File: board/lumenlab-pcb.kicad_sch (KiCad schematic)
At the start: 19 parts, among them J1 Barrel_Jack, SW1 SW_SPST, U1 MP2338

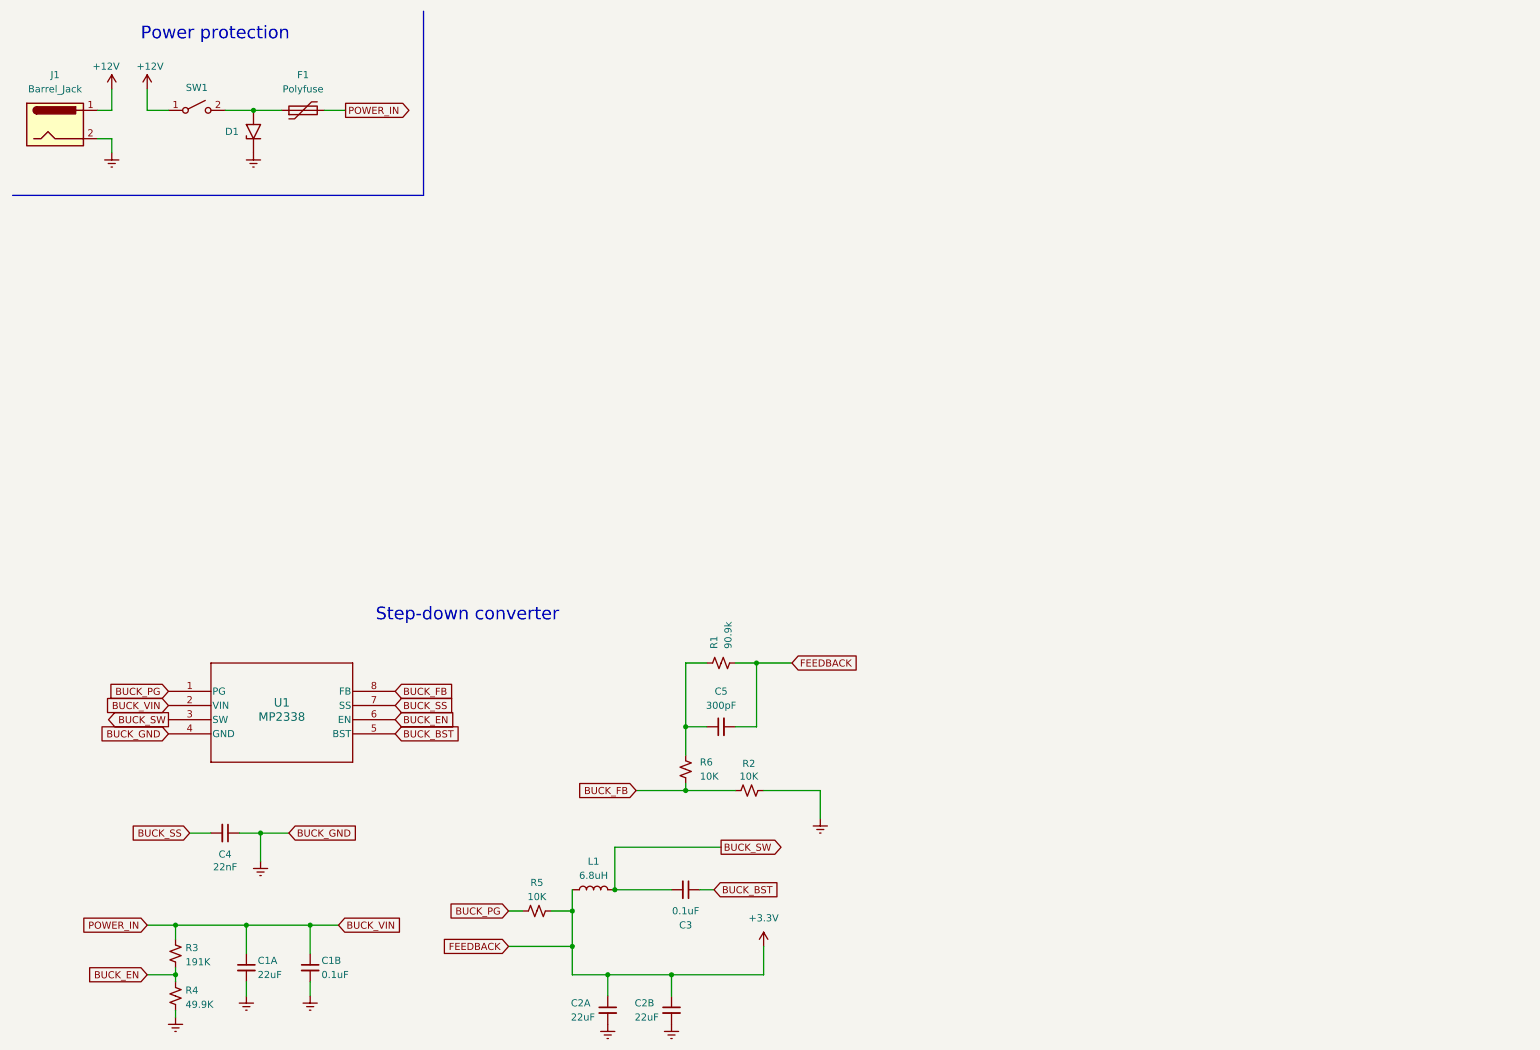
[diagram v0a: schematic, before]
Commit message: Move vendor lib
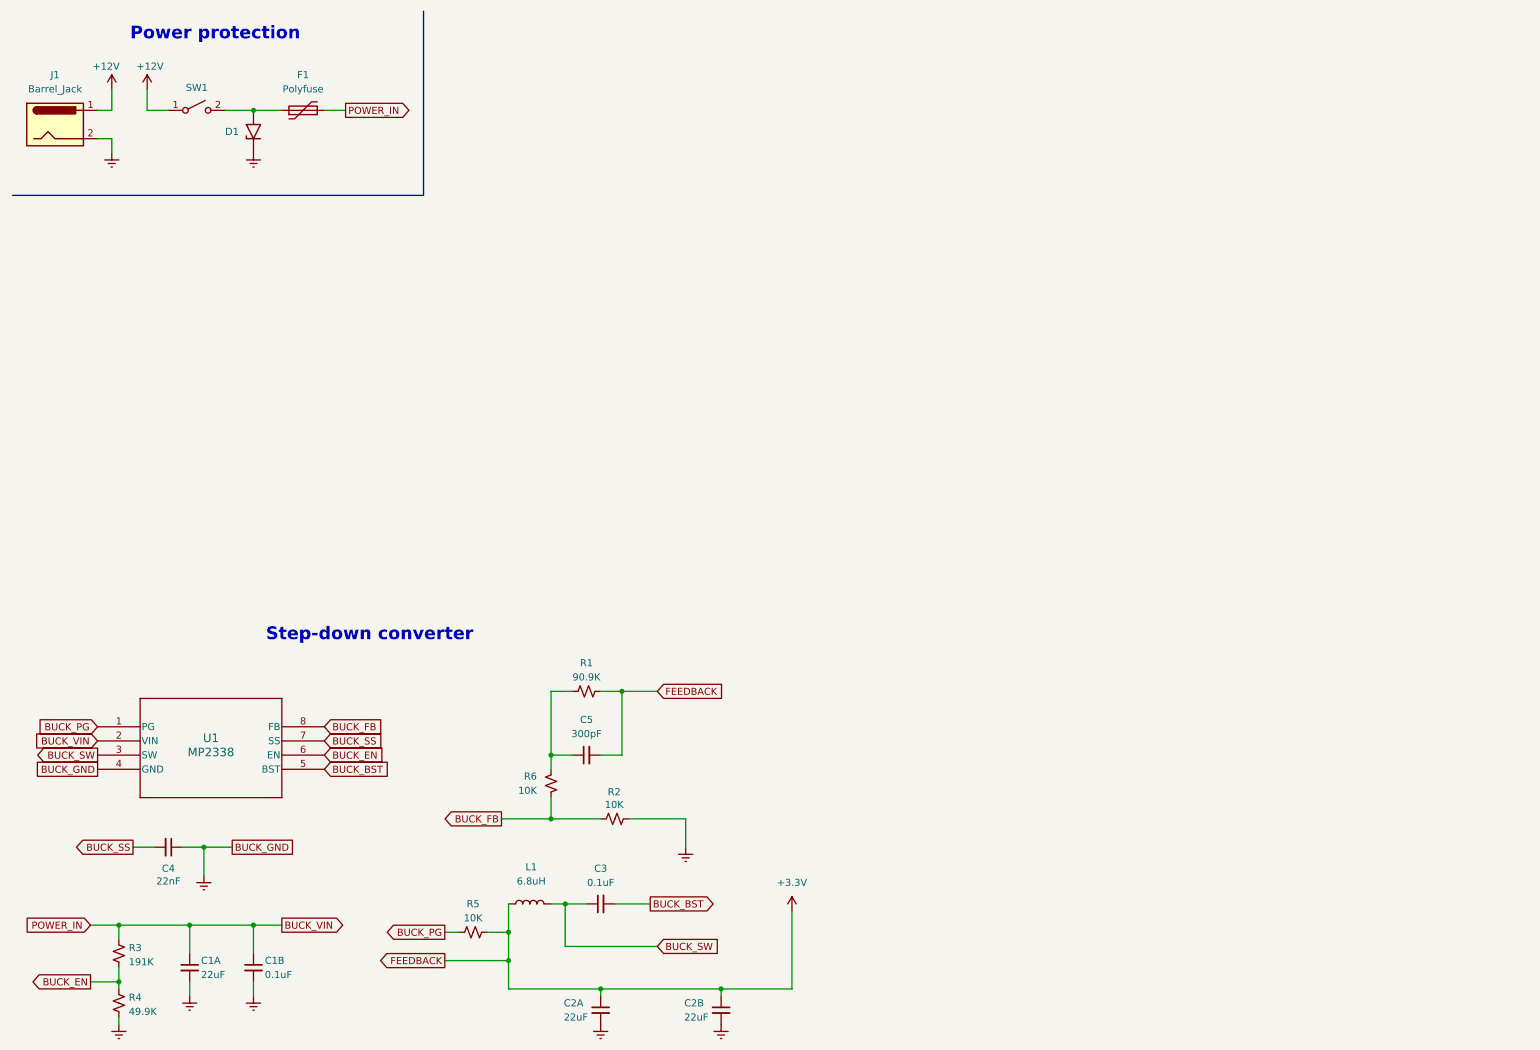
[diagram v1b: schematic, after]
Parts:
- R1: value 90.9k -> 90.9K
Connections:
- net BUCK_BST: now also C3.2; no longer C3.1
- net BUCK_SW: now also C3.1; no longer C3.2
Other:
- moved on the sheet: C1A, C1B, C2A, C2B, C3, C4, C5, L1, R2, R3, R4, R5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

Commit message: Finish buck converter schematic
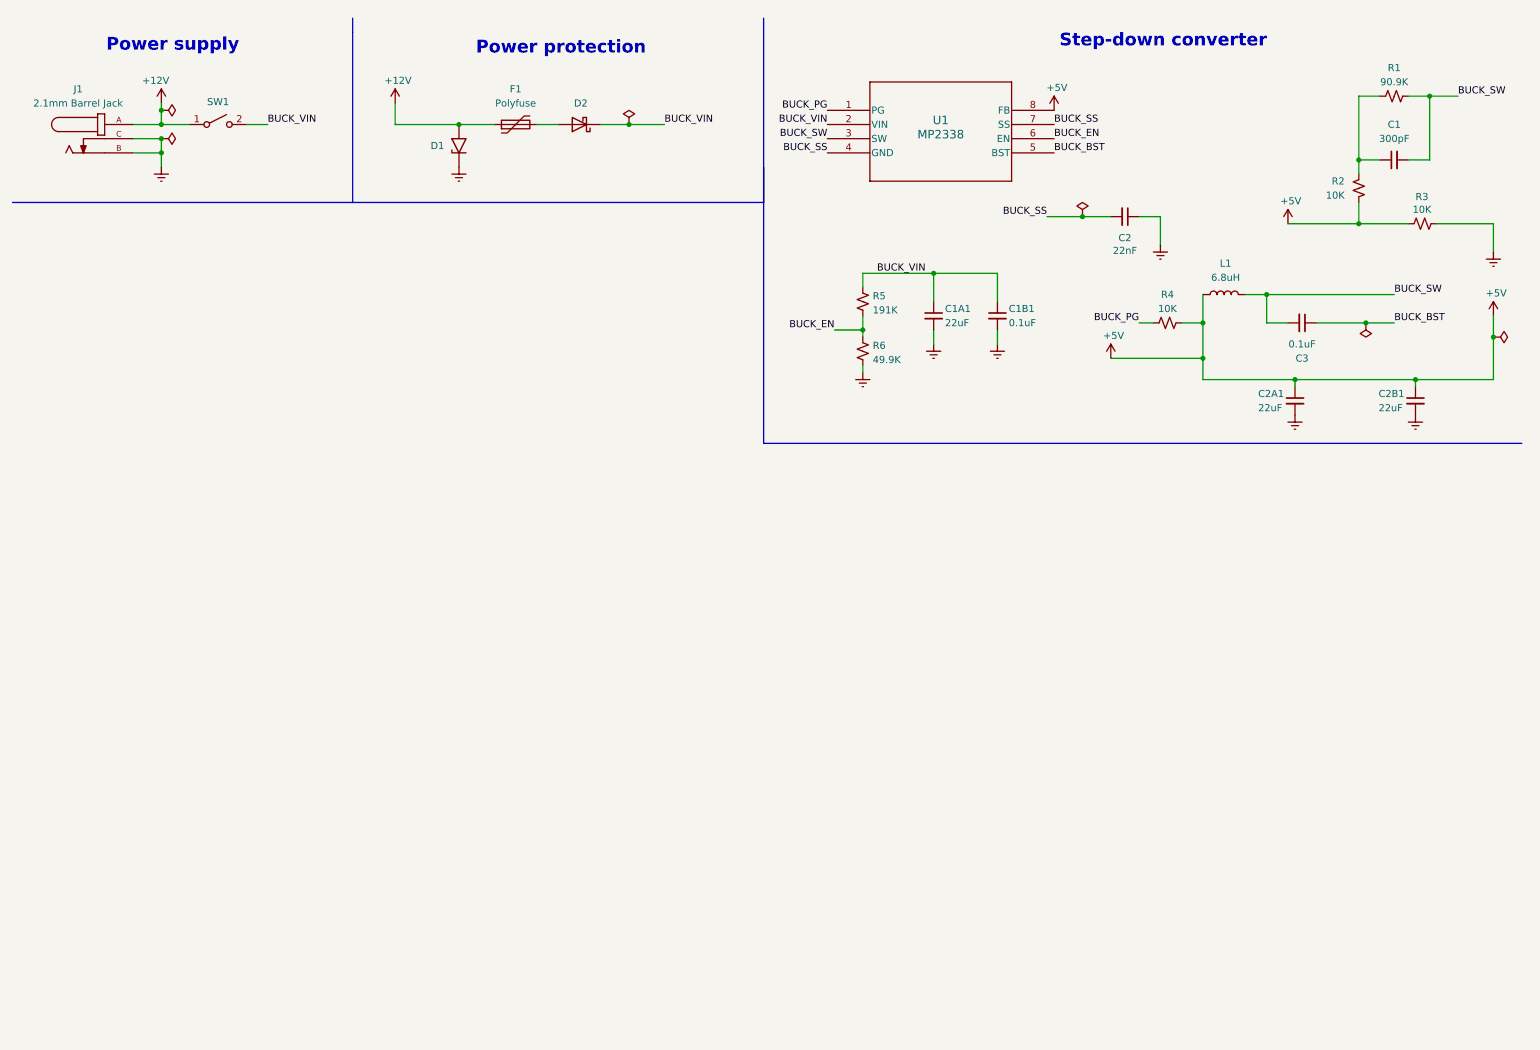
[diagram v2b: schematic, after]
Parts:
- removed J1: Barrel_Jack, symbol Connector:Barrel_Jack
- added D2: SS34, Diode_SMD:D_SMA, symbol Diode:SS34
- added J1: 2.1mm Barrel Jack, 54-00129:TENSILITY_54-00129, symbol 1_Custom_BarrelJack:54-00129
- U1: footprint SOT583_MP2338_MNP -> MP2338:SOT583_MP2338_MNP
- renumbered C5 to C1, C1A to C1A1, C1B to C1B1, C4 to C2, C2A to C2A1, C2B to C2B1, R6 to R2, R2 to R3, R5 to R4, R3 to R5, R4 to R6
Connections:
- net BUCK_FB is gone; now on net +5V: R2.2, R3.1, U1.8 (FB)
- net +12V: now also D1.2 (A2), F1.1, J1.A
- net BUCK_BST: now also C3.1; no longer C3.2
- net BUCK_SS: now also U1.4 (GND)
- net BUCK_SW: now also C1.2, C3.2, R1.2; no longer C3.1
- net BUCK_VIN: now also SW1.2 (B), D2.1 (K); no longer F1.2
- net +3.3V renamed +5V
- net +5V: no longer C1.2, R1.2
- net Earth renamed GND
- net GND: now also J1.B, J1.C; no longer U1.4 (GND)
- new net: D2.2 (A), F1.2
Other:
- note added: "Power supply"
- moved on the sheet: C1, C1A1, C1B1, C2, C2A1, C2B1, C3, D1, F1, L1, R1, R2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

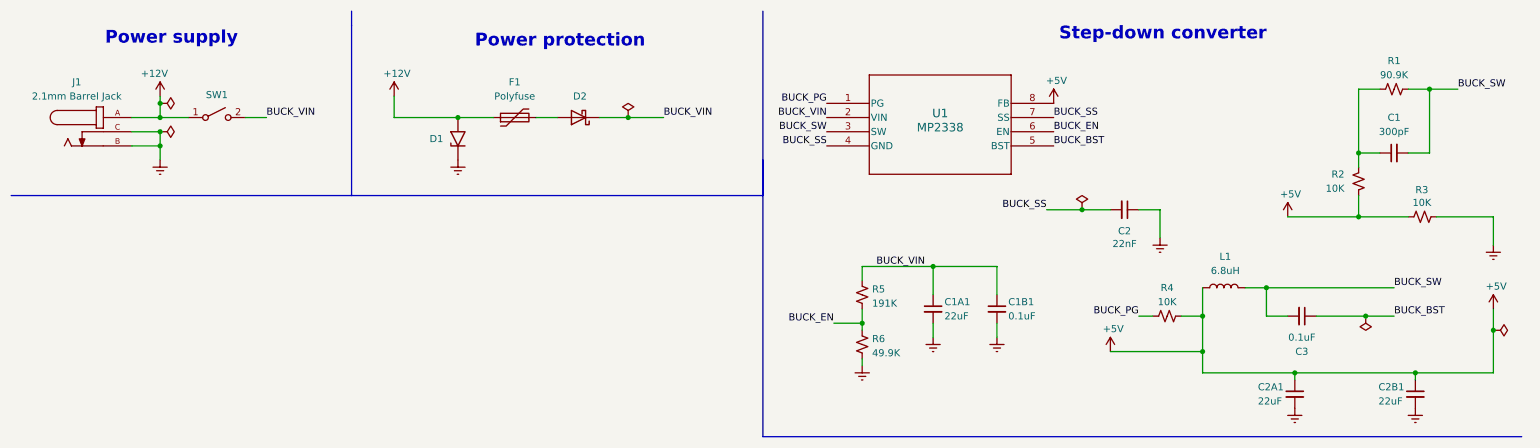
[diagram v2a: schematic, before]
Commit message: Fix mislabeled netlist
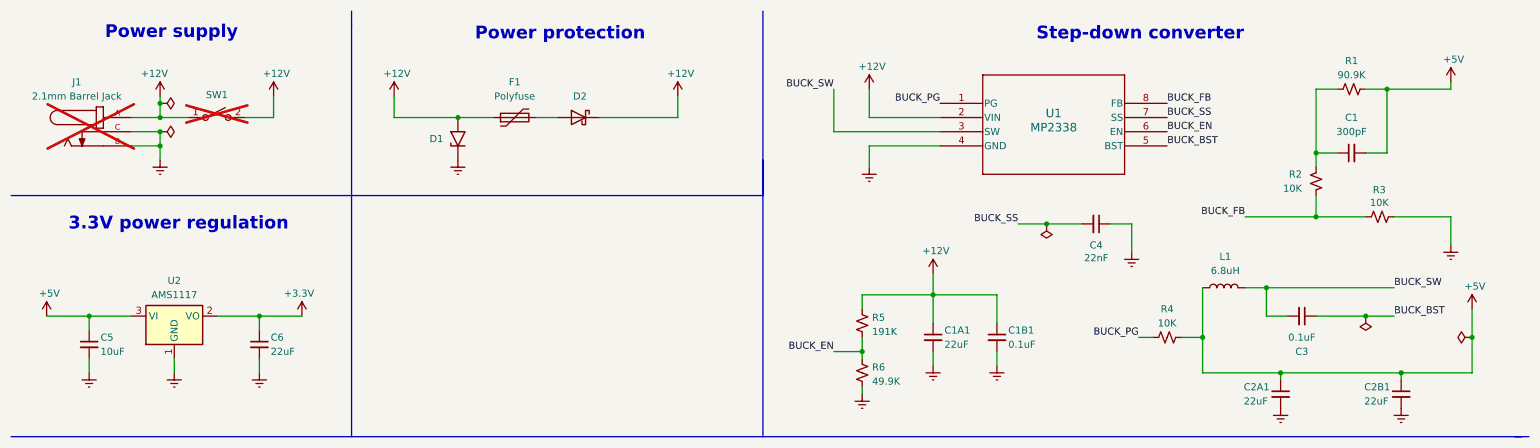
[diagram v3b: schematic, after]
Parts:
- added C5: 10uF, Capacitor_SMD:C_0603_1608Metric_Pad1.08x0.95mm_HandSolder, symbol Device:C_Small
- added C6: 22uF, Capacitor_SMD:C_1210_3225Metric_Pad1.33x2.70mm_HandSolder, symbol Device:C_Small
- added U2: AMS1117, Package_TO_SOT_SMD:SOT-223-3_TabPin2, symbol Regulator_Linear:AMS1117-3.3
- C1, C1B1, C3: footprint (none) -> Capacitor_SMD:C_0603_1608Metric_Pad1.08x0.95mm_HandSolder
- C1A1, C2A1, C2B1: footprint (none) -> Capacitor_SMD:C_1210_3225Metric_Pad1.33x2.70mm_HandSolder
- C4: renamed from C2; footprint (none) -> Capacitor_SMD:C_0603_1608Metric_Pad1.08x0.95mm_HandSolder
- J1: footprint 54-00129:TENSILITY_54-00129 -> Connector_BarrelJack:BarrelJack_GCT_DCJ200-10-A_Horizontal; now not fitted
- L1: footprint (none) -> Inductor_SMD:L_Bourns_SRP5030T
- R1: footprint (none) -> Resistor_SMD:R_0201_0603Metric
- R2, R3, R4, R5, R6: footprint (none) -> Resistor_SMD:R_0603_1608Metric_Pad0.98x0.95mm_HandSolder
- SW1: now not fitted
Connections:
- net BUCK_VIN is gone; now on net +12V: C1A1.1, C1B1.1, D2.1 (K), R5.1, SW1.2 (B), U1.2 (VIN)
- net +5V: now also C1.2, R1.2, C5.1, U2.3 (VI); no longer R2.2, R3.1, U1.8 (FB)
- net BUCK_SS: no longer U1.4 (GND)
- net BUCK_SW: no longer C1.2, R1.2
- net GND: now also U1.4 (GND), C5.2, C6.2, U2.1 (GND)
- new net +3.3V: C6.1, U2.2 (VO)
- new net BUCK_FB: R2.2, R3.1, U1.8 (FB)
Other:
- note added: "3.3V power regulation"
- moved on the sheet: C1, C1A1, C1B1, C2A1, C2B1, C4, D2, R1, R2, R3, R4, R5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

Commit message: Add ESP32 to schematic
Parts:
- added U3: ESP32-WROOM-32D, RF_Module:ESP32-WROOM-32D, symbol RF_Module:ESP32-WROOM-32D
- U1: footprint MP2338:SOT583_MP2338_MNP -> SOT583_MP2338_MNP
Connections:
- net +3.3V: now also U3.2 (VDD)
- net GND: now also U3.1 (GND), U3.15 (GND), U3.38 (GND), U3.39 (GND)

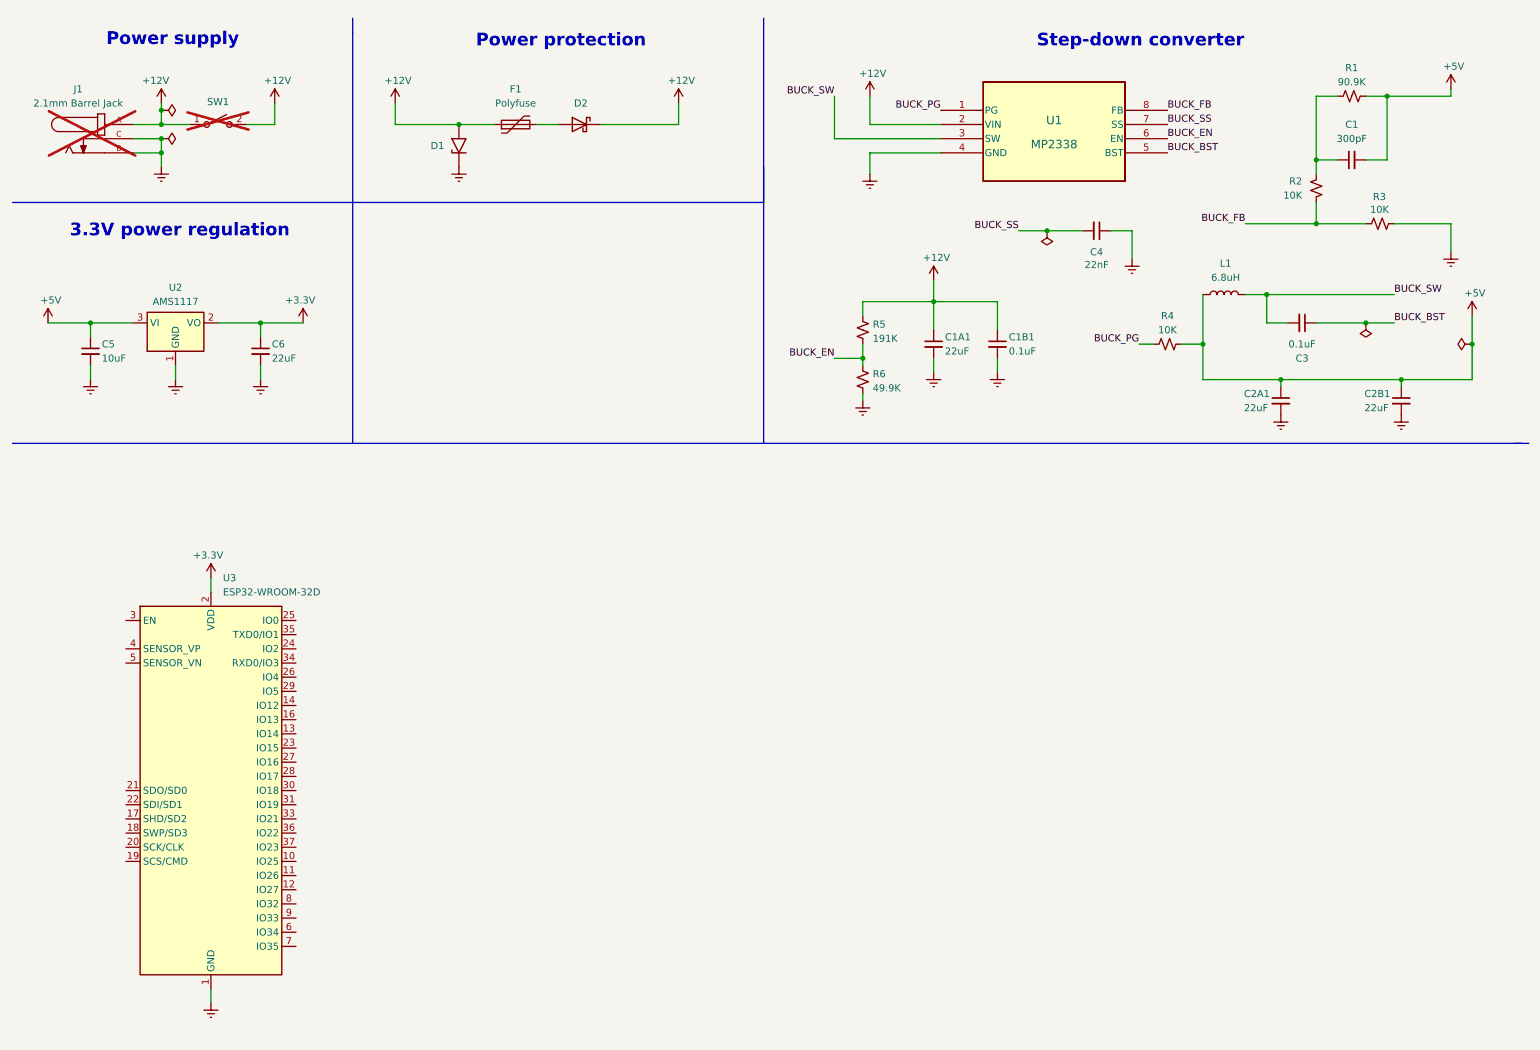
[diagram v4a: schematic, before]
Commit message: Add ESP32 to schematic
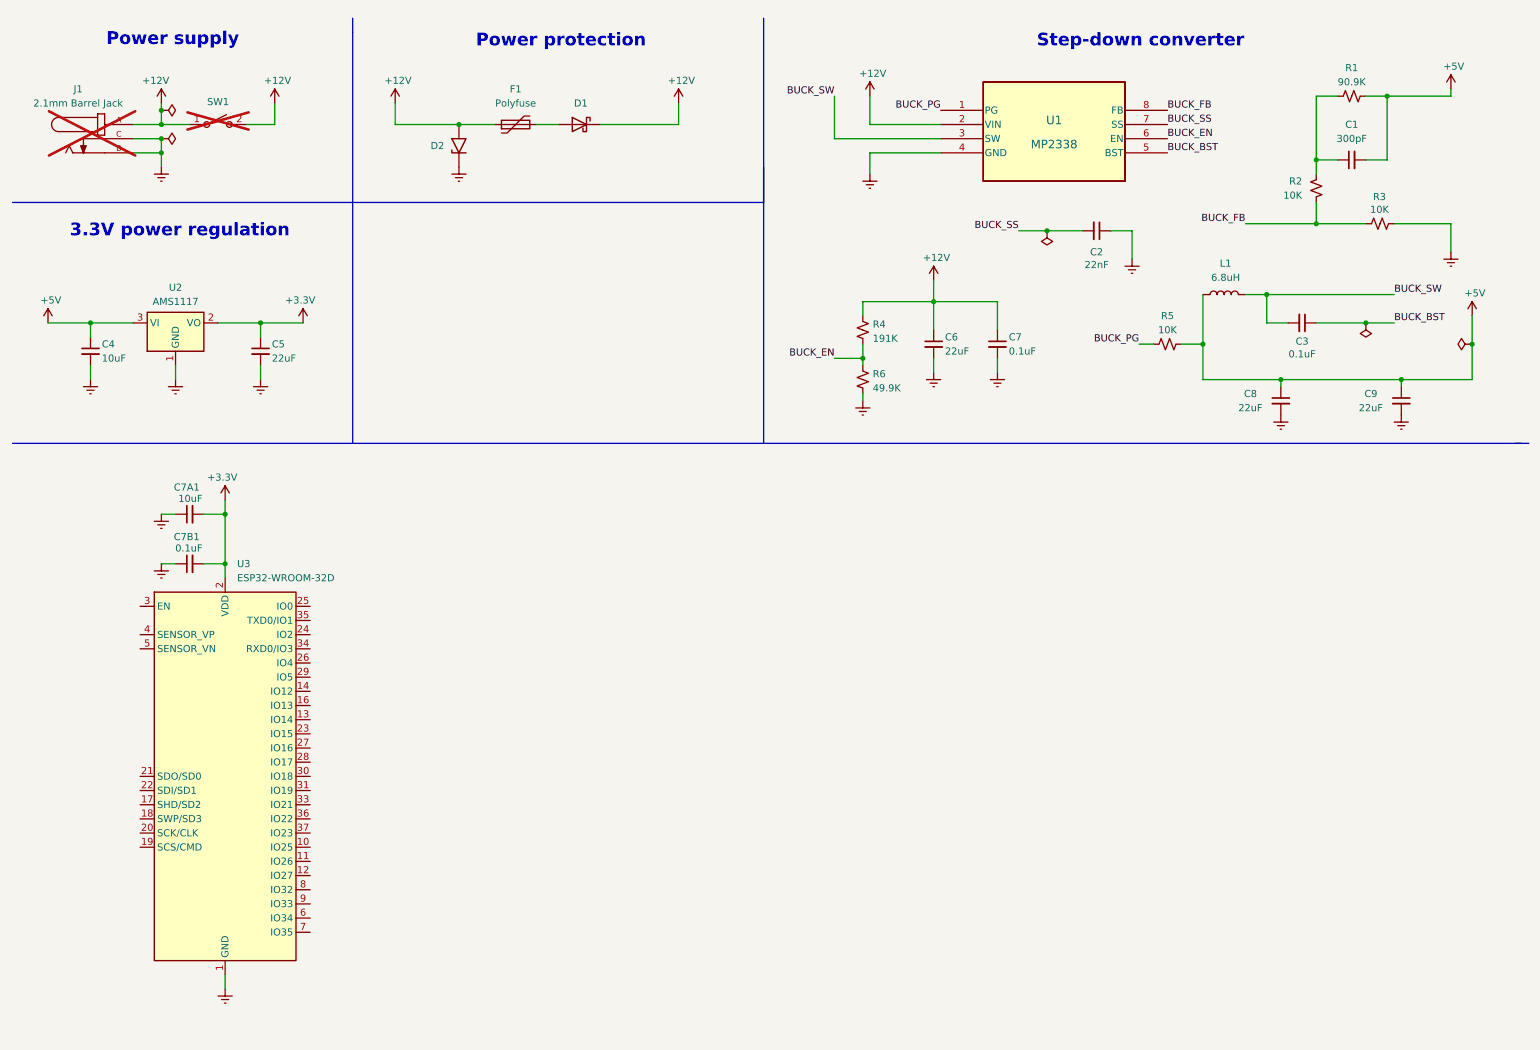
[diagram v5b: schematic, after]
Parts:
- added C7A1: 10uF, Capacitor_SMD:C_1210_3225Metric_Pad1.33x2.70mm_HandSolder, symbol Device:C_Small
- added C7B1: 0.1uF, Capacitor_SMD:C_1210_3225Metric_Pad1.33x2.70mm_HandSolder, symbol Device:C_Small
- renumbered C4 to C2, C5 to C4, C6 to C5, C1A1 to C6, C1B1 to C7, C2A1 to C8, C2B1 to C9, D2 to D1, D1 to D2, R5 to R4, R4 to R5
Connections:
- net +3.3V: now also C7A1.2, C7B1.2
- net GND: now also C7A1.1, C7B1.1
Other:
- moved on the sheet: U3
